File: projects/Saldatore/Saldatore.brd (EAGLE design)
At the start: 160 x 100 mm, 28 parts, among them IC1 7805TV, IC2 LM358N, Q1 IRF540, Q2 2N2905, T1 TIP73

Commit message: in lavoro saldatore.
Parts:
- removed C1, C2: (no value), rcl:C025-025X050
- removed HEATER: (no value), con-phoenix-smkdsp:SMKDSP_1,5/3
- removed IC1: 7805TV, linear:TO220V
- removed TEMP: (no value), Connectors:HDR-02/RA
- added D2: 5v1-2W, diode_MOD:DO41Z10
- added R4: 47-2W, rcl:0204/7
- added SOLDERING: (no value), con-lstb:MA05-1
- R1: value (none) -> 270
- R12, R3: device rcl:RTRIM3339P -> rcl:RTRIM64W
- R2: value (none) -> 10k
- moved C4 140.6 mm to (-53.3, 94.0), turned to 270 degrees
- moved R11 140.6 mm to (-50.8, 96.5), turned to 270 degrees
- moved C3 131.2 mm to (11.4, 128.3), turned to 0 degrees
- moved R12 123.3 mm to (-54.6, 86.4), turned to 180 degrees
- moved 1K 114.8 mm to (15.2, 124.5), turned to 270 degrees
- moved 10K 113.6 mm to (14.0, 130.8)
- moved R3 111.9 mm to (11.4, 120.7), turned to 0 degrees
- moved C5 111.4 mm to (-55.9, 94.0)
- moved R2 108.8 mm to (-54.6, 78.7), turned to 180 degrees
- moved IC2 106.2 mm to (3.81, 121.9)
- moved C6 105.7 mm to (-44.5, 71.1)
- moved IN 105.7 mm to (-45.7, 63.5)
- moved R1 105.6 mm to (-54.6, 73.7)
- moved Q1 103.4 mm to (-63.5, 76.2)
- moved R7 102.4 mm to (-38.1, 96.5), turned to 90 degrees
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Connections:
- net N$21 renamed ENC_CLK
- net N$22 renamed ENC_DT
- net N$23 renamed ENC_SW
- net N$24 renamed 3V3
- removed net 5V: 10K.2, C2.1, IC1.3, U$1.JP2.8
- new net 5V1: 10K.2, D2.C, R4.1, U$1.JP2.8
- net 24V: now also R4.2, SOLDERING.1; no longer C1.1, HEATER.3, IC1.1
- net GND: now also D2.A, SOLDERING.3, SOLDERING.5; no longer C1.2, C2.2, HEATER.1, IC1.2, TEMP.1
- net HEATER-: now also SOLDERING.2; no longer HEATER.2
- net TEMP+: now also SOLDERING.4; no longer TEMP.2
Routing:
- net GND: track 129.6 -> 74.9 mm
- net HEATER-: track 47.0 -> 0.00 mm
- net N$9: track 8.89 -> 54.6 mm
- net N$3: track 26.7 -> 7.62 mm
- net N$5: track 8.15 -> 22.9 mm
- net N$6: track 17.8 -> 5.08 mm
- net N$8: track 30.5 -> 22.9 mm
- net 5V: track 7.62 -> 0.00 mm
- net N$7: track 19.1 -> 25.4 mm
- net 24V: track 67.4 -> 73.7 mm
- net 5V1: track 0.00 -> 2.54 mm
- net TEMP+: track 7.64 -> 10.2 mm
- net N$1: track 8.89 -> 7.62 mm
- net ADC_3.3: track 6.35 -> 5.08 mm
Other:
- board outline removed

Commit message: in lavoro messa su scheda saldatore.
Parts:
- moved SOLDERING 126.9 mm to (-58.4, 63.5), turned to 90 degrees
- moved 10K 54.2 mm to (-27.9, 96.5), turned to 90 degrees
- moved C3 50.3 mm to (-25.4, 94.0), turned to 90 degrees
- moved 1K 45.5 mm to (-21.6, 97.8), turned to 0 degrees
- moved D2 44.4 mm to (-20.3, 100.3), turned to 0 degrees
- moved IC2 42.3 mm to (-19.1, 86.4), turned to 180 degrees
- moved R3 39.6 mm to (-17.8, 94.0), turned to 90 degrees
- moved U$1 26.8 mm to (-17.8, 66.0), turned to 90 degrees
- moved Q1 3.81 mm to (-63.5, 80.0)
- moved R1 3.81 mm to (-54.6, 77.5)
- moved R2 3.81 mm to (-54.6, 82.5)
- moved R12 2.84 mm to (-55.9, 88.9), turned to 270 degrees
- moved Q2 2.54 mm to (-43.2, 87.6)
- moved T1 2.54 mm to (-33.0, 87.6)
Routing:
- net TEMP+: track 10.2 -> 113.0 mm, vias 0 -> 2
- net GND: track 74.9 -> 167.0 mm
- net PWM: track 0.00 -> 64.1 mm
- net ADC_3.3: track 5.08 -> 61.6 mm
- net 5V1: track 2.54 -> 51.4 mm
- net HEATER-: track 0.00 -> 26.7 mm
- net N$8: track 22.9 -> 44.5 mm, vias 0 -> 2
- net N$7: track 25.4 -> 22.9 mm
- net N$6: track 5.08 -> 2.54 mm
- net 24V: track 73.7 -> 71.1 mm
- net N$9: track 54.6 -> 53.3 mm

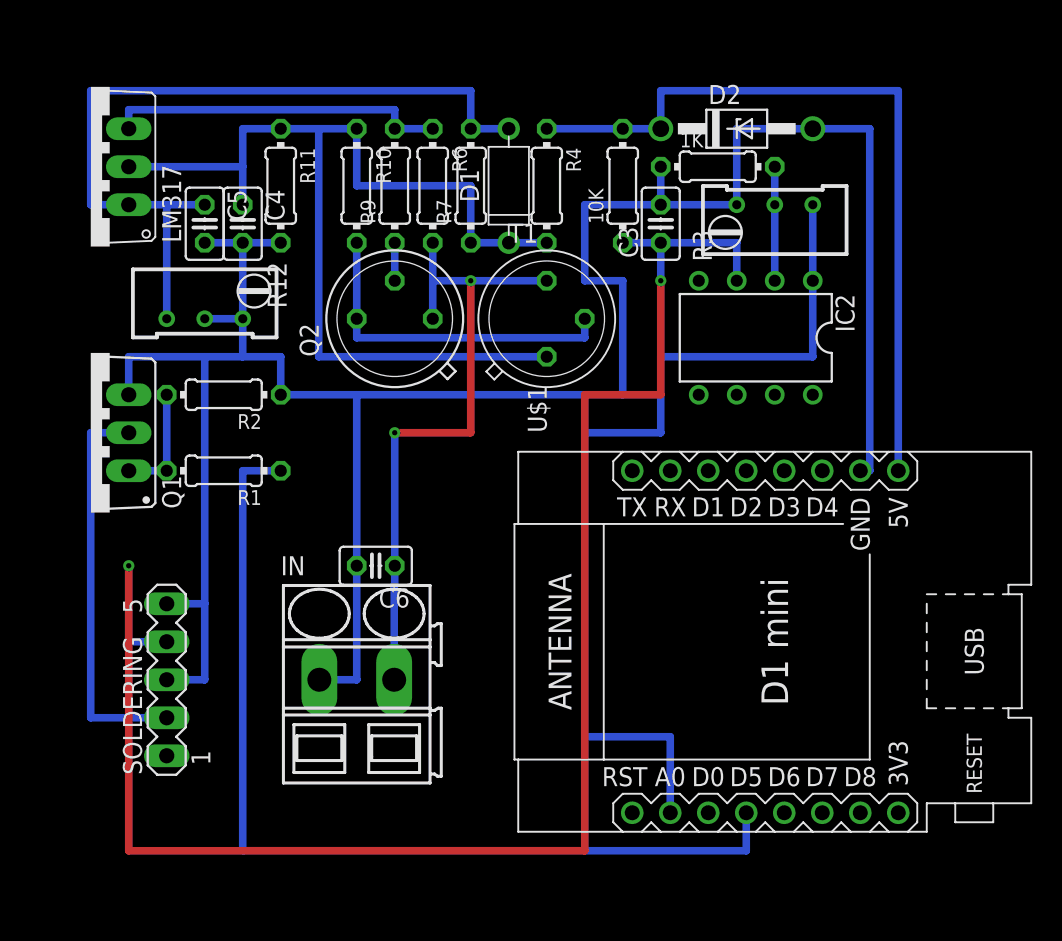
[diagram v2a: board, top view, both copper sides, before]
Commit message: terminato schema saldatore. esportate immagini.
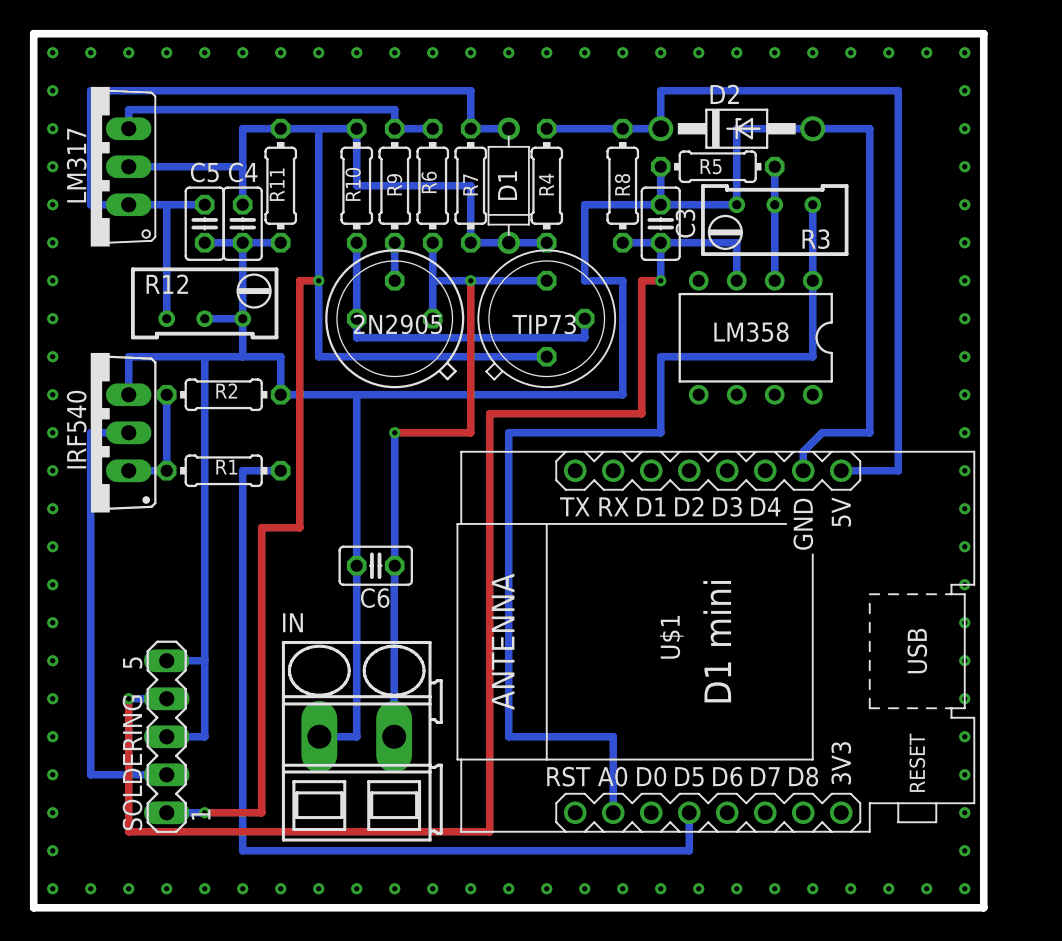
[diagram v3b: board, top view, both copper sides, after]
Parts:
- R5: value (none) -> 1k
- R8: value (none) -> 10K
- moved IN 3.81 mm to (-45.7, 59.7)
- moved SOLDERING 3.81 mm to (-58.4, 59.7)
- moved U$1 3.81 mm to (-21.6, 66.0)
- renumbered 10K to R8, 1K to R5, IC2 to LM358, Q1 to IRF540, Q2 to 2N2905, T1 to TIP73
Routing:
- net 24V: track 71.1 -> 116.8 mm, vias 0 -> 2
- net TEMP+: track 113.0 -> 96.5 mm
- net GND: track 167.0 -> 177.7 mm
- net ADC_3.3: track 61.6 -> 67.9 mm
- net PWM: track 64.1 -> 60.3 mm
- net N$8: track 44.5 -> 48.3 mm
- net HEATER-: track 26.7 -> 30.5 mm
- net 5V1: track 51.4 -> 55.2 mm
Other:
- board outline added: 63.5 x 58.4 mm
